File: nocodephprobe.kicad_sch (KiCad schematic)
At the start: 37 parts, among them J1 RF1-01 BNC, J2 10K, Q1 2N7002, SW1 SW_SPST, U1 LMV358a, U2 ICL7106CPL, U3 MCP1501T-10E/CHY, U4 VI-302-DP-RC-S, U5 78l05

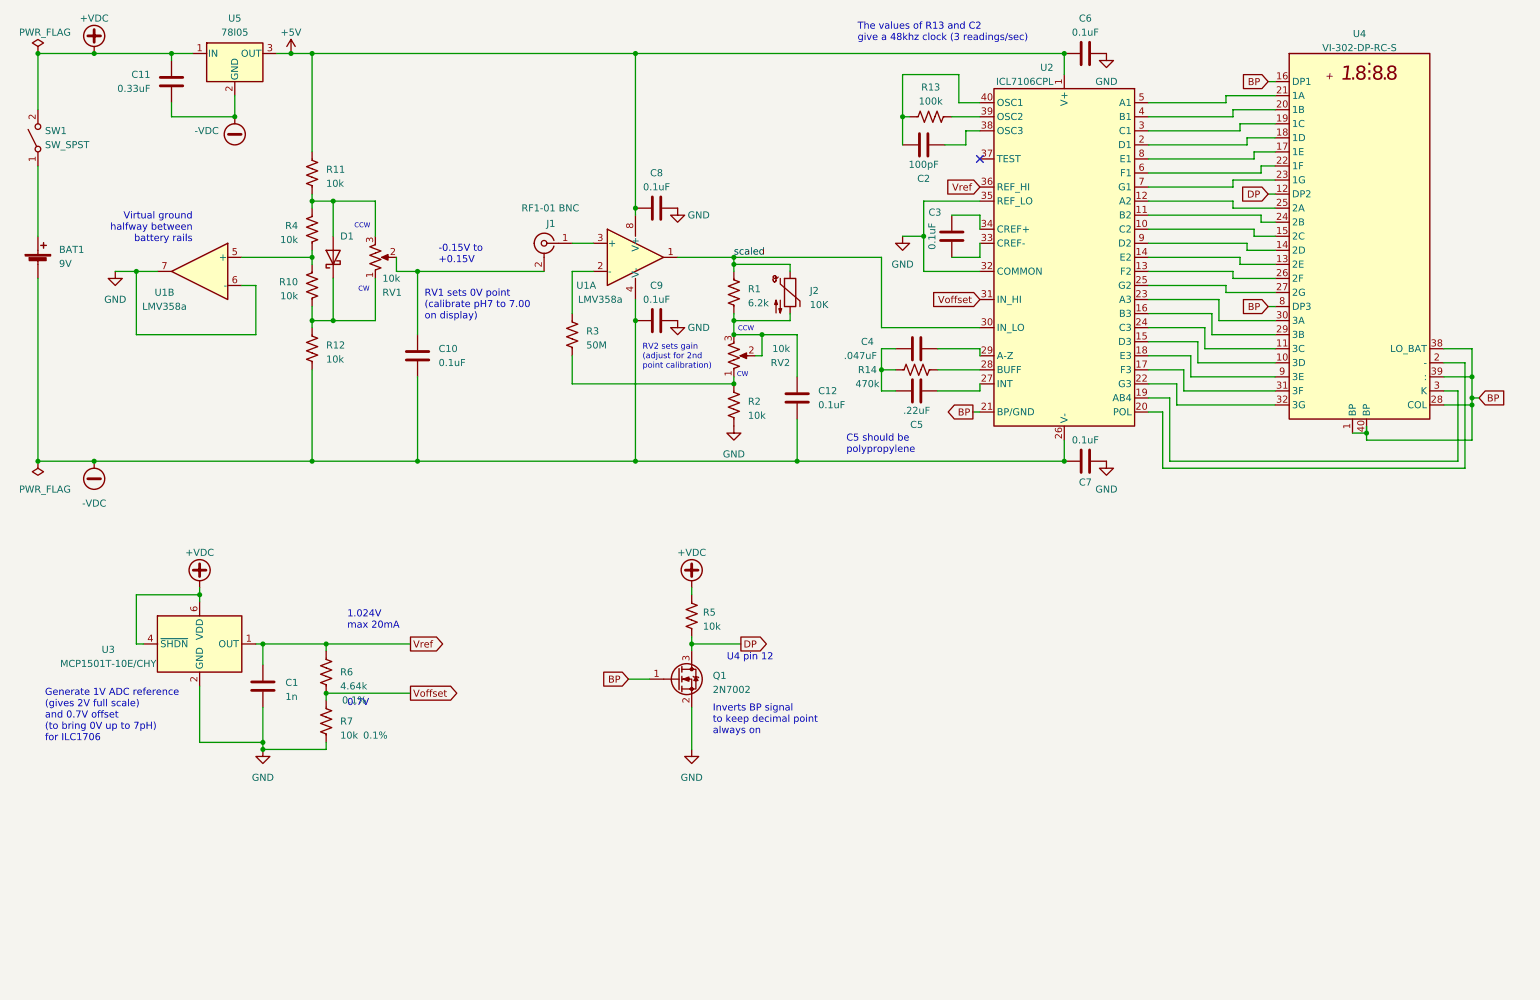
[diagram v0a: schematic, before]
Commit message: schematic: simplify power and decoupling
The big change is switch from the lmv358a to the tlv272:

- TLV272 can operate from up to 16.5V supply, which means we can run it
  directly from the 9V battery (no 7805 or zeners required)
  - It has better typical Vos (500uV), Input Offset Current (1pA), and
    Input Bias Current (1PA)
  - It has worse max offset specs (Vos=5mV, Iio/Iib = 60pA), but they
    are still acceptable
  - Only a little more expensive (the Diodes Incorporated version on
    Digikey is $0.66 for single quantity)
  - Iio and Iib are the same, so there is no point/need for big feedback
    resistor.

Also added a lpf to the output of the amp (R3, C13) with 160hz cutoff...
the 7106 only updates at 3hz anyway, so might as well take advantage of
the low bandwidth requirements to keep noise out. (Chose 10k and 0.1uF
because I'm already using those everywhere)

Routed other bypass caps to gnd instead of -VDC for easier PCB routing.

C12 now bypasses to the negative input of U1A instead of to -VDC to make
sure high frequencies are actually being included in negative feedback.
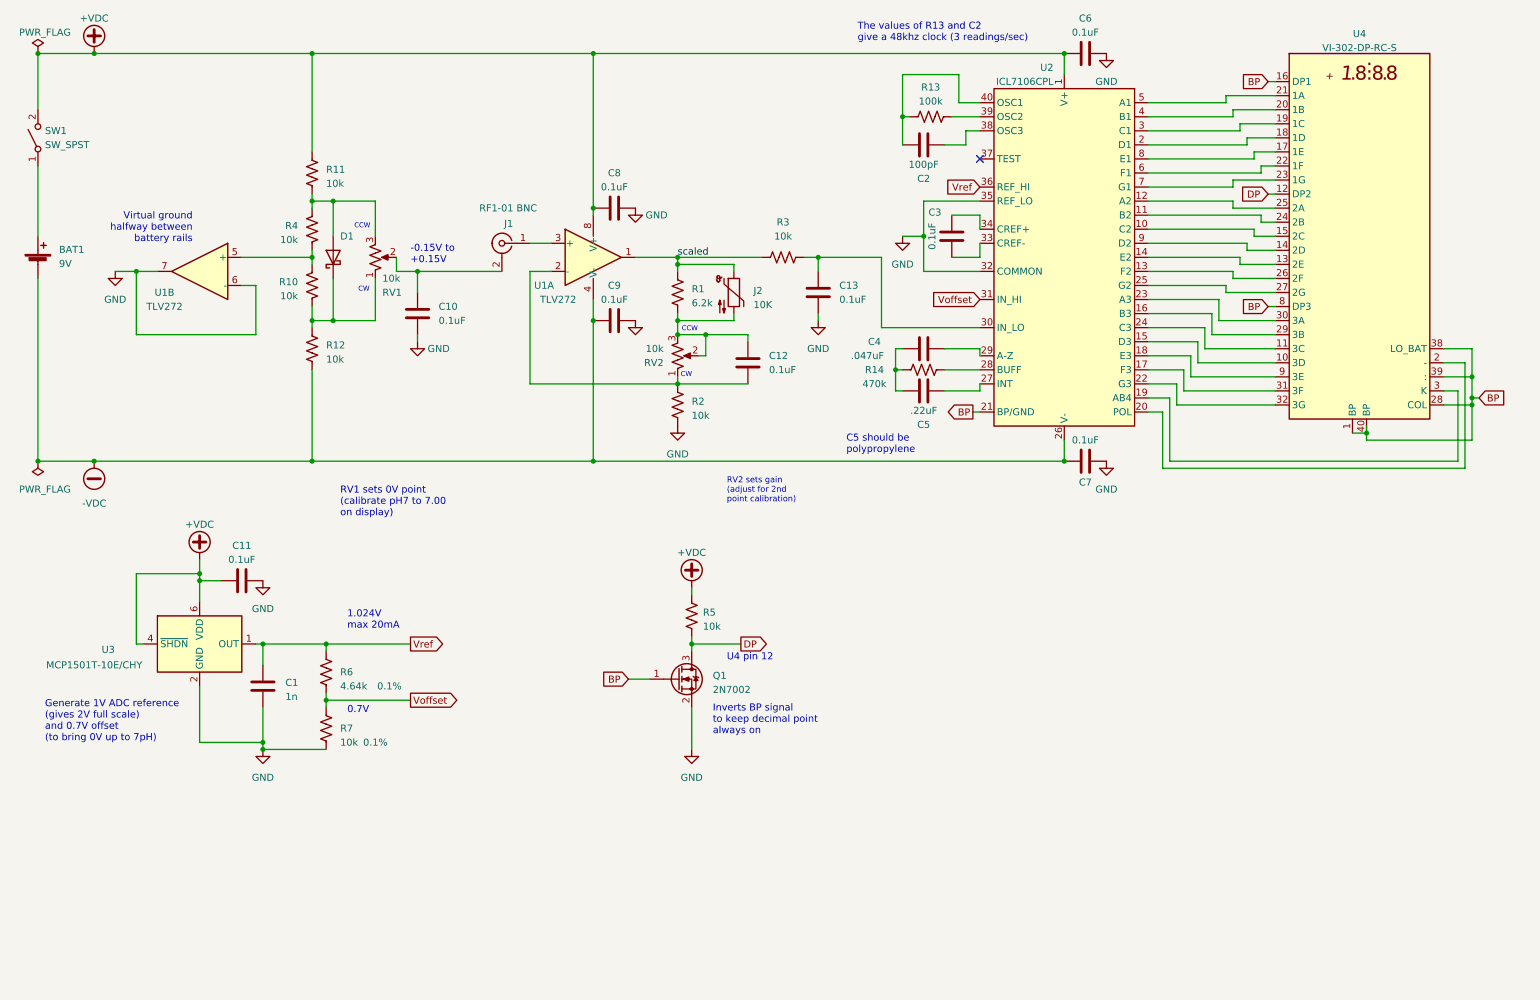
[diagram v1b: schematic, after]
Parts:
- removed U5: 78l05, Package_TO_SOT_SMD:SOT-89-3_Handsoldering, symbol Regulator_Linear:L7805
- added C13: 0.1uF, Capacitor_SMD:C_0805_2012Metric_Pad1.18x1.45mm_HandSolder, symbol Device:C
- C11: value 0.33uF -> 0.1uF
- R3: value 50M -> 10k
- U1: value LMV358a -> TLV272
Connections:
- net +5V is gone; now on net +VDC: C6.1, C8.1, R11.2, U1.8 (V+), U2.1 (V+)
- net +VDC: now also C11.1; no longer C11.2
- net -VDC: no longer C10.1, C11.1, C12.1
- net GND: now also C10.1, C11.2, C13.1
- net scaled: now also R3.1; no longer U2.30 (IN_LO)
- net at U1.2 (-): now also C12.1, R2.2, RV2.1; no longer R3.1
- new net: C13.2, R3.2, U2.30 (IN_LO)
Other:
- note added: "Generate 1V ADC reference (gives 2V full scale) and 0.7V offset (to bring 0V up to 7pH)"
- note removed: "Generate 1V ADC reference (gives 2V full scale) and 0.7V offset (to bring 0V up to 7pH) for ILC1706"
- moved on the sheet: C10, C12, C4, C5, C8, C9, J1, J2, R1, R14, R2, R7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

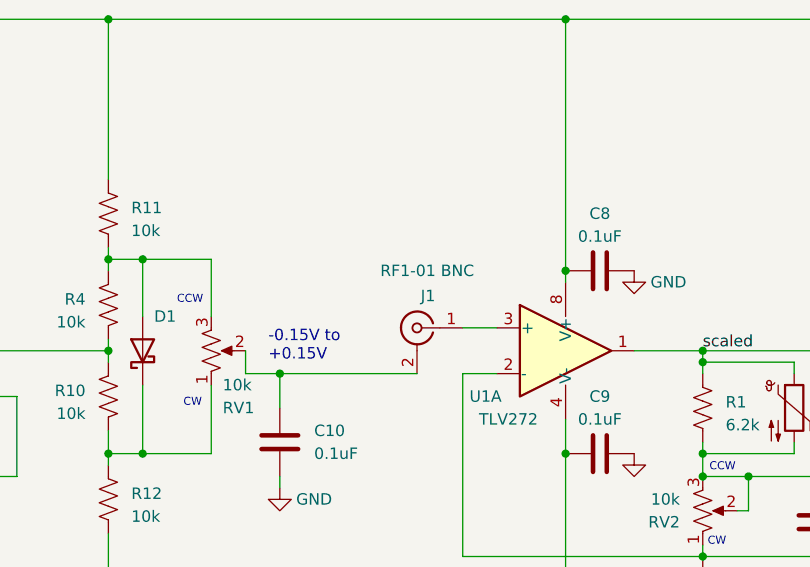
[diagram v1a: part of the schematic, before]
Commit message: pcb: route improved power and headers
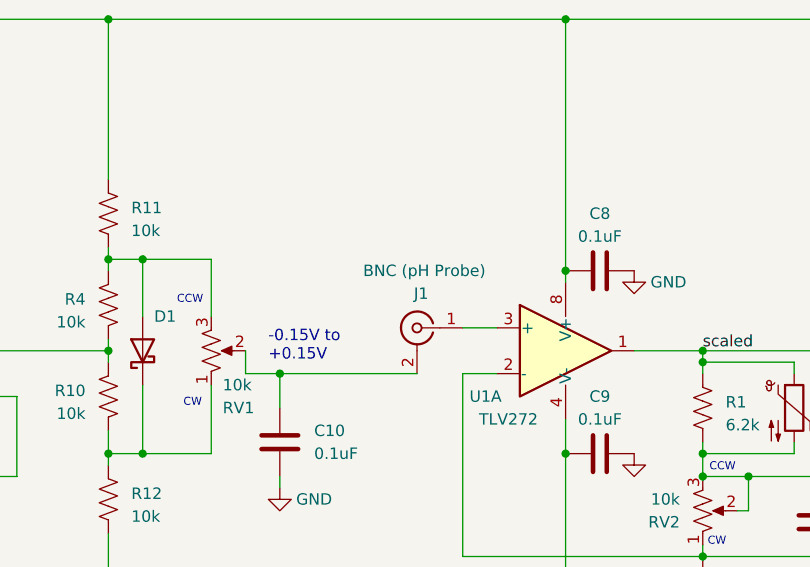
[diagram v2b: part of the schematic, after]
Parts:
- BAT1: footprint Connector_Molex:Molex_KK-396_A-41792-0002_1x02_P3.96mm_Horizontal -> Connector_JST:JST_XH_B2B-XH-A_1x02_P2.50mm_Vertical
- J1: value RF1-01 BNC -> BNC (pH Probe)
- RV1, RV2: footprint Connector_PinHeader_2.54mm:PinHeader_1x03_P2.54mm_Horizontal -> Connector_JST:JST_XH_B3B-XH-A_1x03_P2.50mm_Vertical
- SW1: footprint Connector_PinHeader_2.54mm:PinHeader_2x01_P2.54mm_Vertical -> Connector_JST:JST_XH_B2B-XH-A_1x02_P2.50mm_Vertical
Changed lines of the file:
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@@
       (effects (font (size 1.27 1.27)) (justify right))
     )
-    (property "Footprint" "Connector_PinHeader_2.54mm:PinHeader_2x01_P2.54mm_Vertical" (at 16.51 41.91 0)
+    (property "Footprint" "Connector_JST:JST_XH_B2B-XH-A_1x02_P2.50mm_Vertical" (at 16.51 41.91 0)
       (effects (font (size 1.27 1.27)) hide)
     )
@@
       (effects (font (size 1.27 1.27)) (justify right))
     )
-    (property "Footprint" "Connector_PinHeader_2.54mm:PinHeader_1x03_P2.54mm_Horizontal" (at 132.08 81.28 0)
+    (property "Footprint" "Connector_JST:JST_XH_B3B-XH-A_1x03_P2.50mm_Vertical" (at 132.08 81.28 0)
       (effects (font (size 1.27 1.27)) hide)
     )
@@
       (effects (font (size 1.27 1.27)) (justify left))
     )
-    (property "Footprint" "Connector_Molex:Molex_KK-396_A-41792-0002_1x02_P3.96mm_Horizontal" (at 16.51 63.246 90)
+    (property "Footprint" "Connector_JST:JST_XH_B2B-XH-A_1x02_P2.50mm_Vertical" (at 16.51 63.246 90)
       (effects (font (size 1.27 1.27)) hide)
     )
@@
       (effects (font (size 1.27 1.27)) (justify left))
     )
-    (property "Footprint" "Connector_PinHeader_2.54mm:PinHeader_1x03_P2.54mm_Horizontal" (at 77.47 63.5 0)
+    (property "Footprint" "Connector_JST:JST_XH_B3B-XH-A_1x03_P2.50mm_Vertical" (at 77.47 63.5 0)
       (effects (font (size 1.27 1.27)) hide)
     )
@@
   (symbol (lib_id "Connector:Conn_Coaxial") (at 100.33 60.96 0) (mirror y) (unit 1)
     (in_bom yes) (on_board yes) (dnp no)
-    (property "Reference" "J1" (at 102.362 57.404 0)
-      (effects (font (size 1.27 1.27)) (justify left))
-    )
-    (property "Value" "RF1-01 BNC" (at 106.68 54.61 0)
-      (effects (font (size 1.27 1.27)) (justify left))
-    )
+    (property "Reference" "J1" (at 101.6 57.15 0)
+      (effects (font (size 1.27 1.27)) (justify left))
+    )
+    (property "Value" "BNC (pH Probe)" (at 107.95 54.61 0)
+      (effects (font (size 1.27 1.27)) (justify left))
+    )

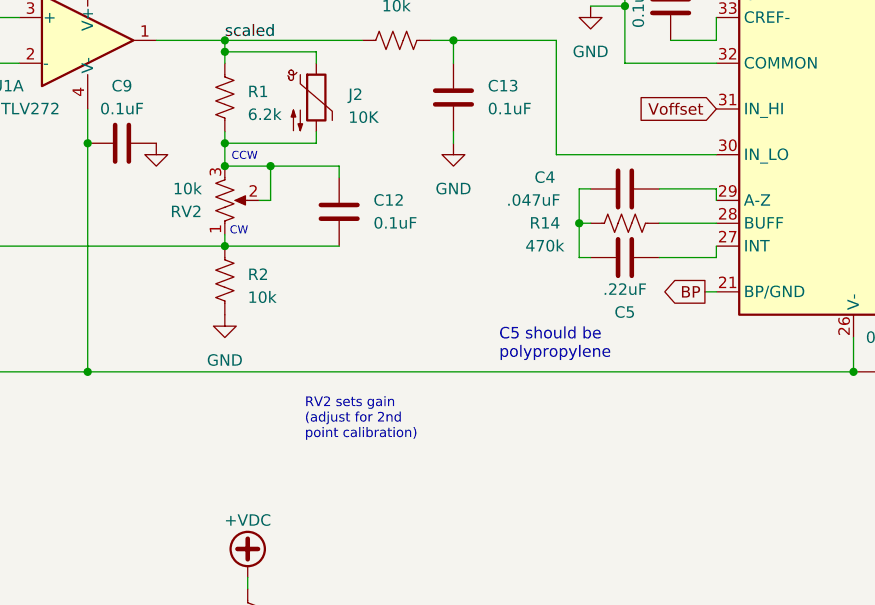
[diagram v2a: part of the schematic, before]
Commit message: pcb: use 2-pin header for RV2
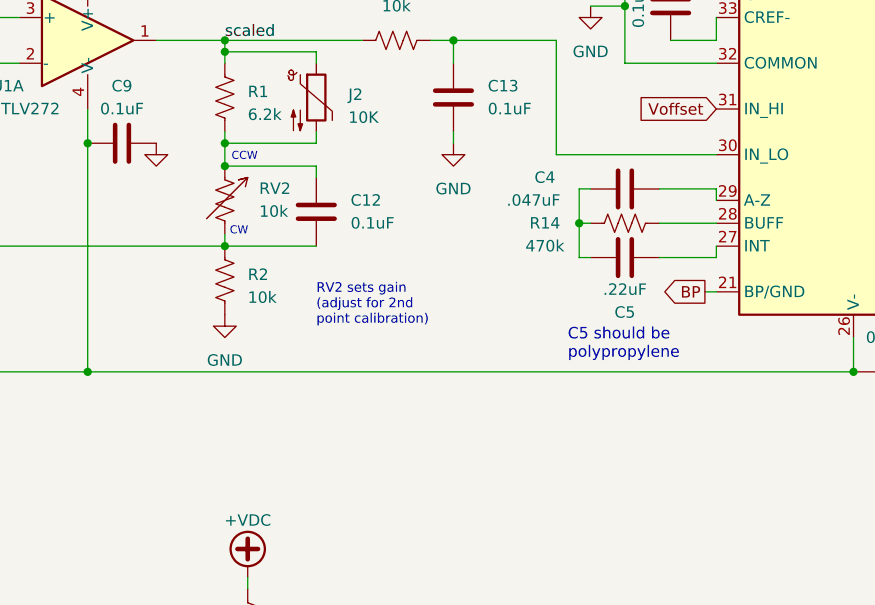
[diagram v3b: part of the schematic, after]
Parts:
- removed RV2: 10k, Connector_JST:JST_XH_B3B-XH-A_1x03_P2.50mm_Vertical, symbol Device:R_Potentiometer_US
- added RV2: 10k, Connector_JST:JST_XH_B2B-XH-A_1x02_P2.50mm_Vertical, symbol Device:R_Variable_US
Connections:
- net at C12.1, R2.2, U1.2 (-): now also RV2.2
- net at C12.2, J2.5, R1.1: now also RV2.1
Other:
- moved on the sheet: C12
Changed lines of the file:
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@@
   (junction (at 275.59 88.9) (diameter 0) (color 0 0 0 0)
   )
+  (junction (at 132.08 64.77) (diameter 0) (color 0 0 0 0)
+  )
+  (junction (at 69.85 74.93) (diameter 0) (color 0 0 0 0)
+  )
+  (junction (at 66.04 63.5) (diameter 0) (color 0 0 0 0)
+  )
+  (junction (at 275.59 90.17) (diameter 0) (color 0 0 0 0)
+  )
+  (junction (at 66.04 100.33) (diameter 0) (color 0 0 0 0)
+  )
+  (junction (at 16.51 100.33) (diameter 0) (color 0 0 0 0)
+  )
+  (junction (at 201.93 100.33) (diameter 0) (color 0 0 0 0)
+  )
+  (junction (at 176.53 59.69) (diameter 0) (color 0 0 0 0)
+  )
+  (junction (at 57.15 151.13) (diameter 0) (color 0 0 0 0)
+  )
+  (junction (at 45.72 121.92) (diameter 0) (color 0 0 0 0)
+  )
+  (junction (at 134.62 133.35) (diameter 0) (color 0 0 0 0)
+  )
+  (junction (at 201.93 26.67) (diameter 0) (color 0 0 0 0)
+  )
   (junction (at 132.08 77.47) (diameter 0) (color 0 0 0 0)
   )
-  (junction (at 132.08 64.77) (diameter 0) (color 0 0 0 0)
-  )
-  (junction (at 69.85 74.93) (diameter 0) (color 0 0 0 0)
-  )
-  (junction (at 66.04 63.5) (diameter 0) (color 0 0 0 0)
-  )
-  (junction (at 275.59 90.17) (diameter 0) (color 0 0 0 0)
-  )
-  (junction (at 66.04 100.33) (diameter 0) (color 0 0 0 0)
-  )
-  (junction (at 16.51 100.33) (diameter 0) (color 0 0 0 0)
-  )
-  (junction (at 201.93 100.33) (diameter 0) (color 0 0 0 0)
-  )
-  (junction (at 176.53 59.69) (diameter 0) (color 0 0 0 0)
-  )
-  (junction (at 57.15 151.13) (diameter 0) (color 0 0 0 0)
-  )
-  (junction (at 45.72 121.92) (diameter 0) (color 0 0 0 0)
-  )
-  (junction (at 134.62 133.35) (diameter 0) (color 0 0 0 0)
-  )
-  (junction (at 201.93 26.67) (diameter 0) (color 0 0 0 0)
-  )
   (junction (at 132.08 74.93) (diameter 0) (color 0 0 0 0)
   )
@@
   )
   (junction (at 45.72 120.65) (diameter 0) (color 0 0 0 0)
-  )
-  (junction (at 137.16 77.47) (diameter 0) (color 0 0 0 0)
   )
   (junction (at 68.58 143.51) (diameter 0) (color 0 0 0 0)
@@
     (stroke (width 0) (type default))
   )
-  (wire (pts (xy 144.78 77.47) (xy 137.16 77.47))
-    (stroke (width 0) (type default))
-  )
   (wire (pts (xy 227.33 80.01) (xy 240.03 80.01))
     (stroke (width 0) (type default))
@@
     (stroke (width 0) (type default))
   )
-  (wire (pts (xy 137.16 77.47) (xy 132.08 77.47))
+  (wire (pts (xy 132.08 77.47) (xy 142.24 77.47))
     (stroke (width 0) (type default))
   )
@@
     (stroke (width 0) (type default))
   )
-  (wire (pts (xy 132.08 86.36) (xy 144.78 86.36))
+  (wire (pts (xy 132.08 86.36) (xy 142.24 86.36))
     (stroke (width 0) (type default))
   )
@@
     (stroke (width 0) (type default))
   )
-  (wire (pts (xy 137.16 81.28) (xy 137.16 77.47))
-    (stroke (width 0) (type default))
-  )
   (wire (pts (xy 270.51 90.17) (xy 275.59 90.17))
     (stroke (width 0) (type default))
@@
     (stroke (width 0) (type default))
   )
-  (wire (pts (xy 144.78 78.74) (xy 144.78 77.47))
+  (wire (pts (xy 142.24 78.74) (xy 142.24 77.47))
     (stroke (width 0) (type default))
   )
@@
   )
   (wire (pts (xy 116.84 26.67) (xy 116.84 54.61))
-    (stroke (width 0) (type default))
-  )
-  (wire (pts (xy 135.89 81.28) (xy 137.16 81.28))
     (stroke (width 0) (type default))
   )
@@
     (effects (font (size 0.889 0.889)) (justify left bottom))
   )
-  (text "C5 should be\npolypropylene" (at 162.56 99.06 0)
+  (text "C5 should be\npolypropylene" (at 170.18 99.06 0)
     (effects (font (size 1.27 1.27)) (justify left bottom))
   )
@@
     (effects (font (size 1.27 1.27)) (justify left bottom))
   )
-  (text "RV2 sets gain\n(adjust for 2nd\npoint calibration)" (at 140.97 107.95 0)
+  (text "RV2 sets gain\n(adjust for 2nd\npoint calibration)" (at 142.24 95.25 0)
     (effects (font (size 1.0668 1.0668)) (justify left bottom))
   )
@@
     )
   )
-  (symbol (lib_id "Device:C") (at 144.78 82.55 180) (unit 1)
+  (symbol (lib_id "Device:C") (at 142.24 82.55 180) (unit 1)
     (in_bom yes) (on_board yes) (dnp no)
-    (property "Reference" "C12" (at 148.59 81.28 0)
+    (property "Reference" "C12" (at 146.05 81.28 0)
       (effects (font (size 1.27 1.27)) (justify right))
     )
-    (property "Value" "0.1uF" (at 148.59 83.82 0)
+    (property "Value" "0.1uF" (at 146.05 83.82 0)
       (effects (font (size 1.27 1.27)) (justify right))
     )
-    (property "Footprint" "Capacitor_SMD:C_0805_2012Metric_Pad1.18x1.45mm_HandSolder" (at 143.8148 78.74 0)
-      (effects (font (size 1.27 1.27)) hide)
-    )
-    (property "Datasheet" "~" (at 144.78 82.55 0)
+    (property "Footprint" "Capacitor_SMD:C_0805_2012Metric_Pad1.18x1.45mm_HandSolder" (at 141.2748 78.74 0)
+      (effects (font (size 1.27 1.27)) hide)
+    )
+    (property "Datasheet" "~" (at 142.24 82.55 0)
       (effects (font (size 1.27 1.27)) hide)
     )
@@
     )
   )
-  (symbol (lib_id "Device:R_Potentiometer_US") (at 132.08 81.28 0) (mirror x) (unit 1)
-    (in_bom yes) (on_board yes) (dnp no)
-    (property "Reference" "RV2" (at 129.54 82.55 0)
-      (effects (font (size 1.27 1.27)) (justify right))
-    )
-    (property "Value" "10k" (at 129.54 80.01 0)
-      (effects (font (size 1.27 1.27)) (justify right))
-    )
-    (property "Footprint" "Connector_JST:JST_XH_B3B-XH-A_1x03_P2.50mm_Vertical" (at 132.08 81.28 0)
-      (effects (font (size 1.27 1.27)) hide)
-    )
-    (property "Datasheet" "~" (at 132.08 81.28 0)
-      (effects (font (size 1.27 1.27)) hide)
-    )
-    (pin "1")
-    (pin "2")
-    (pin "3")
-    (instances
-      (project "nocodephprobe"
-        (path "/2036f74b-8ede-4e4d-84df-8cc119de9ab1"
-          (reference "RV2") (unit 1)
-        )
-      )
-    )
-  )
   (symbol (lib_id "power:GND") (at 85.09 78.74 0) (unit 1)
     (in_bom yes) (on_board yes) (dnp no)
@@
         )
       )
+    )
+  )
+  (symbol (lib_id "Device:R_Variable_US") (at 132.08 81.28 0) (unit 1)
+    (in_bom yes) (on_board yes) (dnp no)
+    (property "Reference" "RV2" (at 135.89 79.9719 0)
+      (effects (font (size 1.27 1.27)) (justify left))
+    )
+    (property "Value" "10k" (at 135.89 82.5119 0)
+      (effects (font (size 1.27 1.27)) (justify left))
+    )
+    (property "Footprint" "Connector_JST:JST_XH_B2B-XH-A_1x02_P2.50mm_Vertical" (at 130.302 81.28 90)
+      (effects (font (size 1.27 1.27)) hide)
+    )
+    (property "Datasheet" "~" (at 132.08 81.28 0)
+      (effects (font (size 1.27 1.27)) hide)
+    )
+    (pin "1")
+    (pin "2")
+    (instances
+      (project "nocodephprobe"
+        (path "/2036f74b-8ede-4e4d-84df-8cc119de9ab1"
+          (reference "RV2") (unit 1)
+        )
+      )
